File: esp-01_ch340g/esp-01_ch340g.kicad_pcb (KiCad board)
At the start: 2 copper layers, 25.4 x 32.4 mm, 5 parts, among them SW1 Flash, SW2 Reset, U1 ESP-01

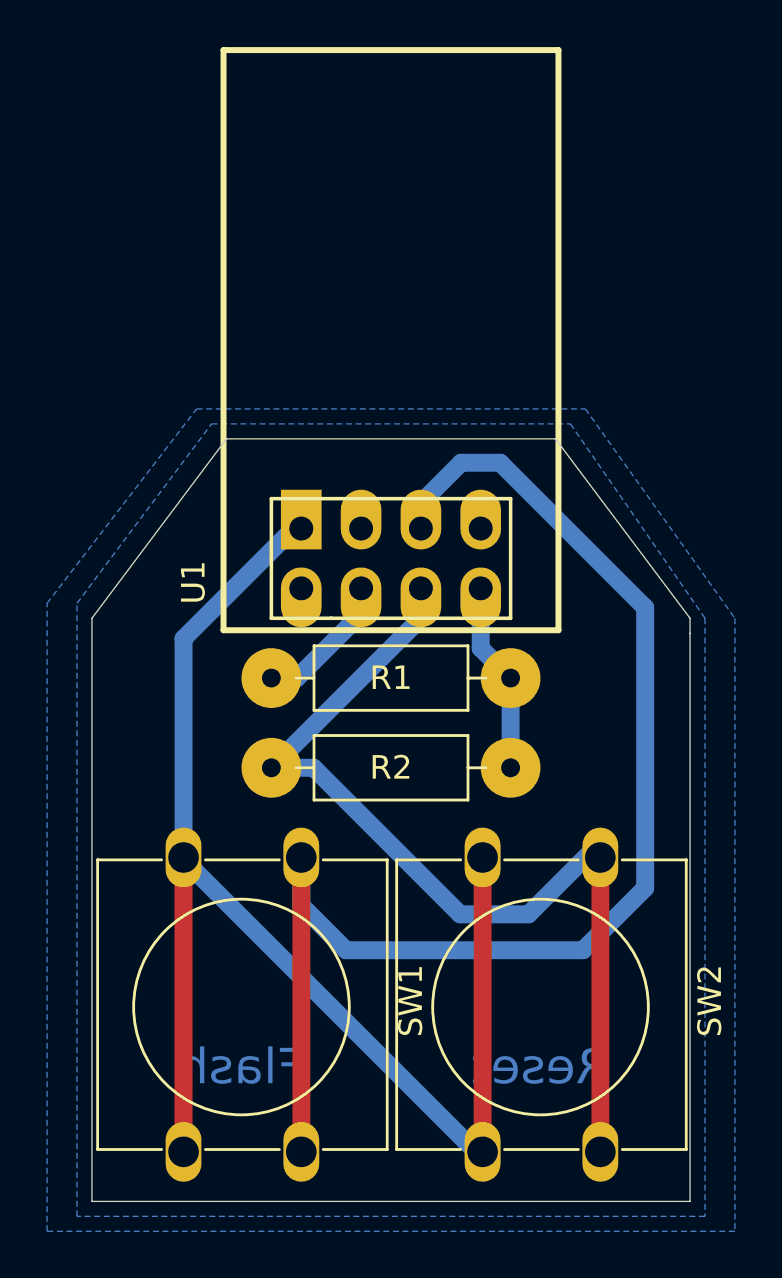
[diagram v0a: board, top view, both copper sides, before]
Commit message: new switches, better 3d
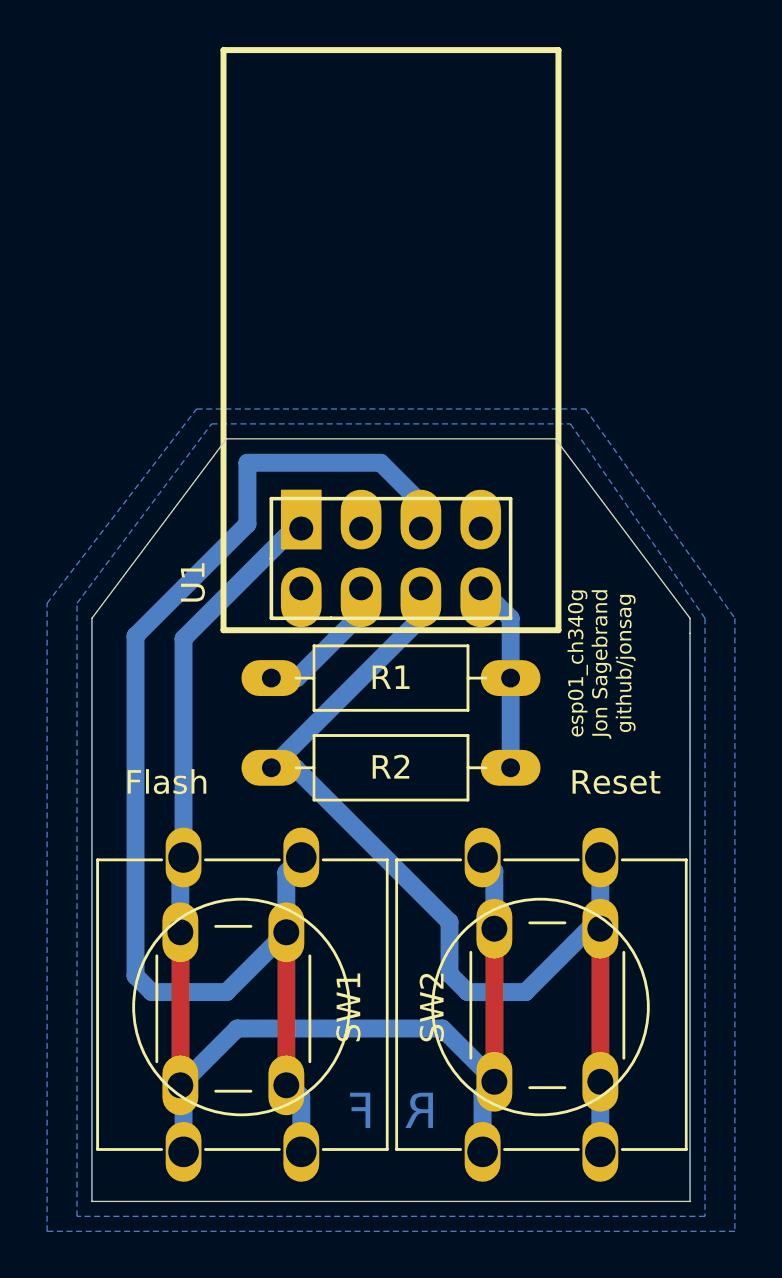
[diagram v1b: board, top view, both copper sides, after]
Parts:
- added SW3: Flash2, My_Misc:SW_PUSH_6mm_large, F.Cu at (153.0, 92.7)
- added SW4: Reset2, My_Misc:SW_PUSH_6mm_large, F.Cu at (166.4, 92.6)
- U1: footprint My_Arduino:ESP-01_large -> My_Arduino:ESP-01_w_pin_socket_large
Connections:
- U1 pad 2: Net-(U1-Pad2) -> unconnected-(U1-Pad2)
- U1 pad 3: Net-(U1-Pad3) -> unconnected-(U1-Pad3)
- U1 pad 7: Net-(U1-Pad7) -> unconnected-(U1-Pad7)
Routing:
- net Net-(R2-Pad2): track 40.1 -> 43.3 mm
- net Net-(SW1-Pad1): track 56.4 -> 53.7 mm
- net GND: track 59.2 -> 57.1 mm
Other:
- net class Default removed
- board text added: "F"
- board text added: "R"
- board text added: "esp01_ch340g Jon Sagebrand github/jonsag"
